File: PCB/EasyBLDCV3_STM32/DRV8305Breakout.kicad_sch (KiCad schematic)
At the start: 30 parts, among them Q1 CSD17573Q5B, Q2 CSD17573Q5B, Q3 CSD17573Q5B, Q4 CSD17573Q5B, Q5 CSD17573Q5B, Q6 CSD17573Q5B

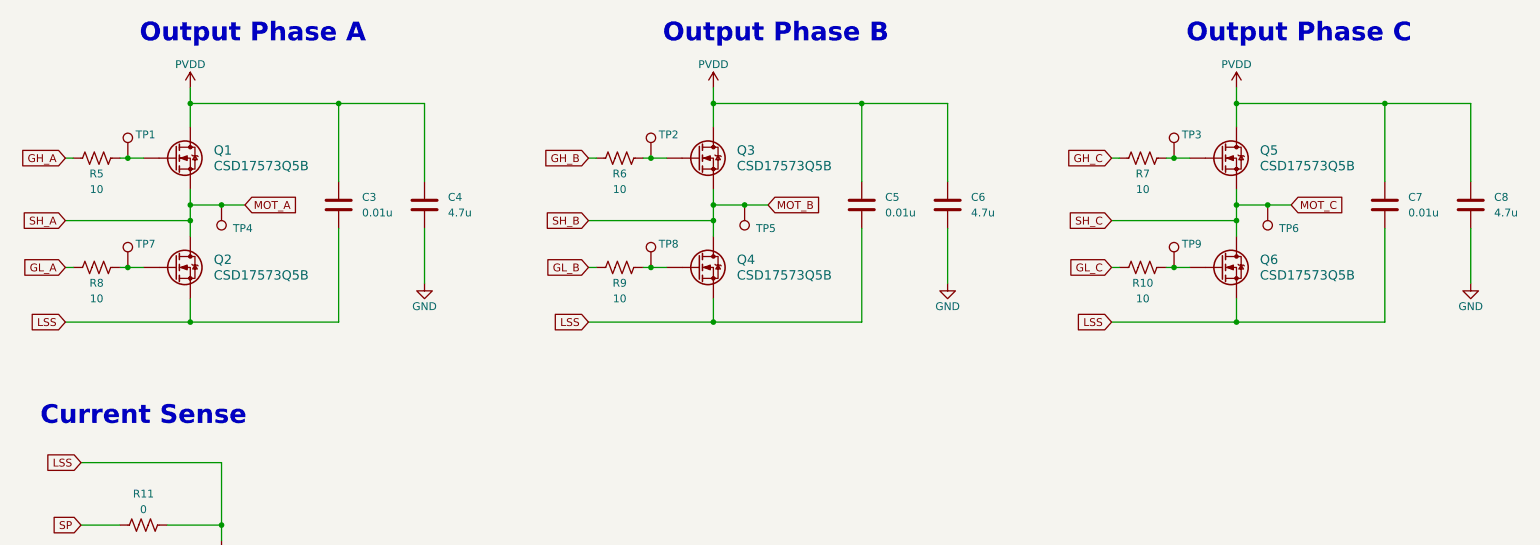
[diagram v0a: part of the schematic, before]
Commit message: Added footprints and began schematic for new gate drive
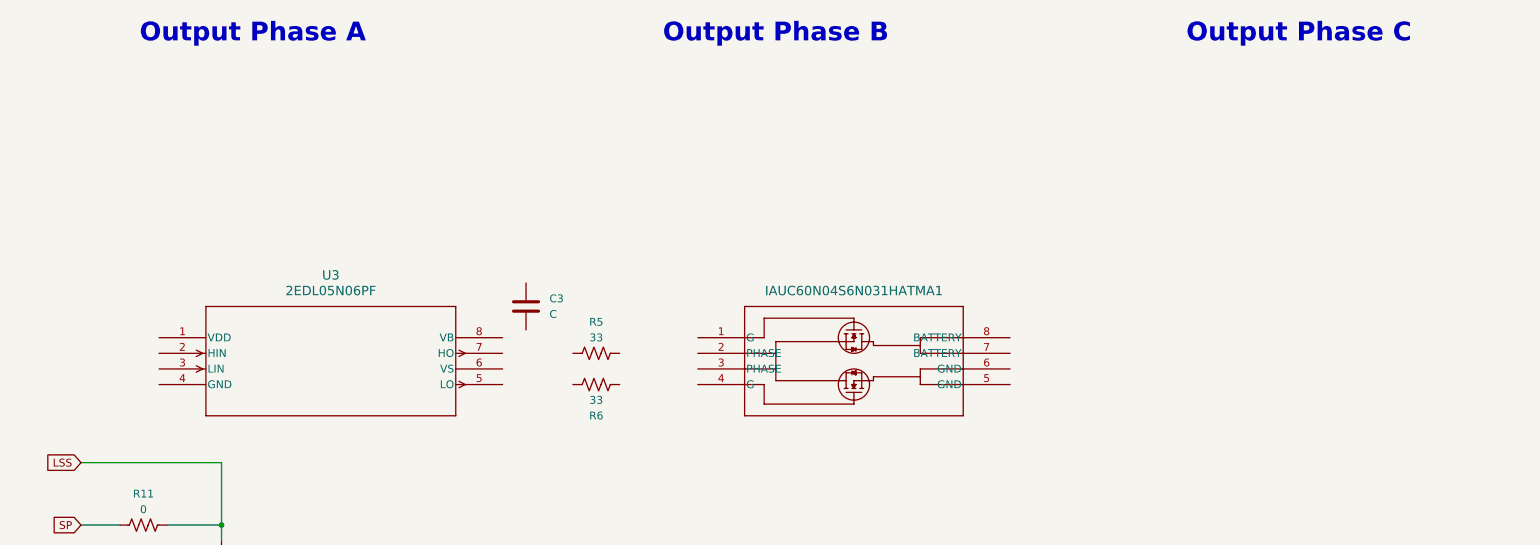
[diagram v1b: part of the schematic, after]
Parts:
- removed C4, C6, C8: 4.7u, Capacitor_SMD:C_1210_3225Metric, symbol Device:C
- removed C5, C7: 0.01u, Capacitor_SMD:C_0805_2012Metric, symbol Device:C
- removed Q1, Q2, Q3, Q4, Q5, Q6: CSD17573Q5B, EasyBLDC:DNK0008A, symbol EasyBLDC:CSD17573Q5B
- removed R10, R7, R8, R9: 10, Resistor_SMD:R_0603_1608Metric, symbol Device:R_US
- removed TP1, TP2, TP3, TP4, TP5, TP6, TP7, TP8, TP9: TestPoint, TestPoint:TestPoint_Pad_D1.5mm, symbol Connector:TestPoint
- added U2: IAUC60N04S6N031HATMA1, PG-TDSON-8-56, symbol EasyBLDC:IAUC60N04S6N031HATMA1
- added U3: 2EDL05N06PF, PG-DSO-8-1_INF, symbol EasyBLDC:2EDL05N06PF
- C3: value 0.01u -> C; footprint Capacitor_SMD:C_0805_2012Metric -> (none)
- R5, R6: value 10 -> 33
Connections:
- net LSS: no longer C3.2
- net GH_A: no longer names the net of R5.1
- net GH_B: no longer names the net of R6.1
- net PVDD: no longer names the net of C3.1
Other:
- note removed: "Current Sense"

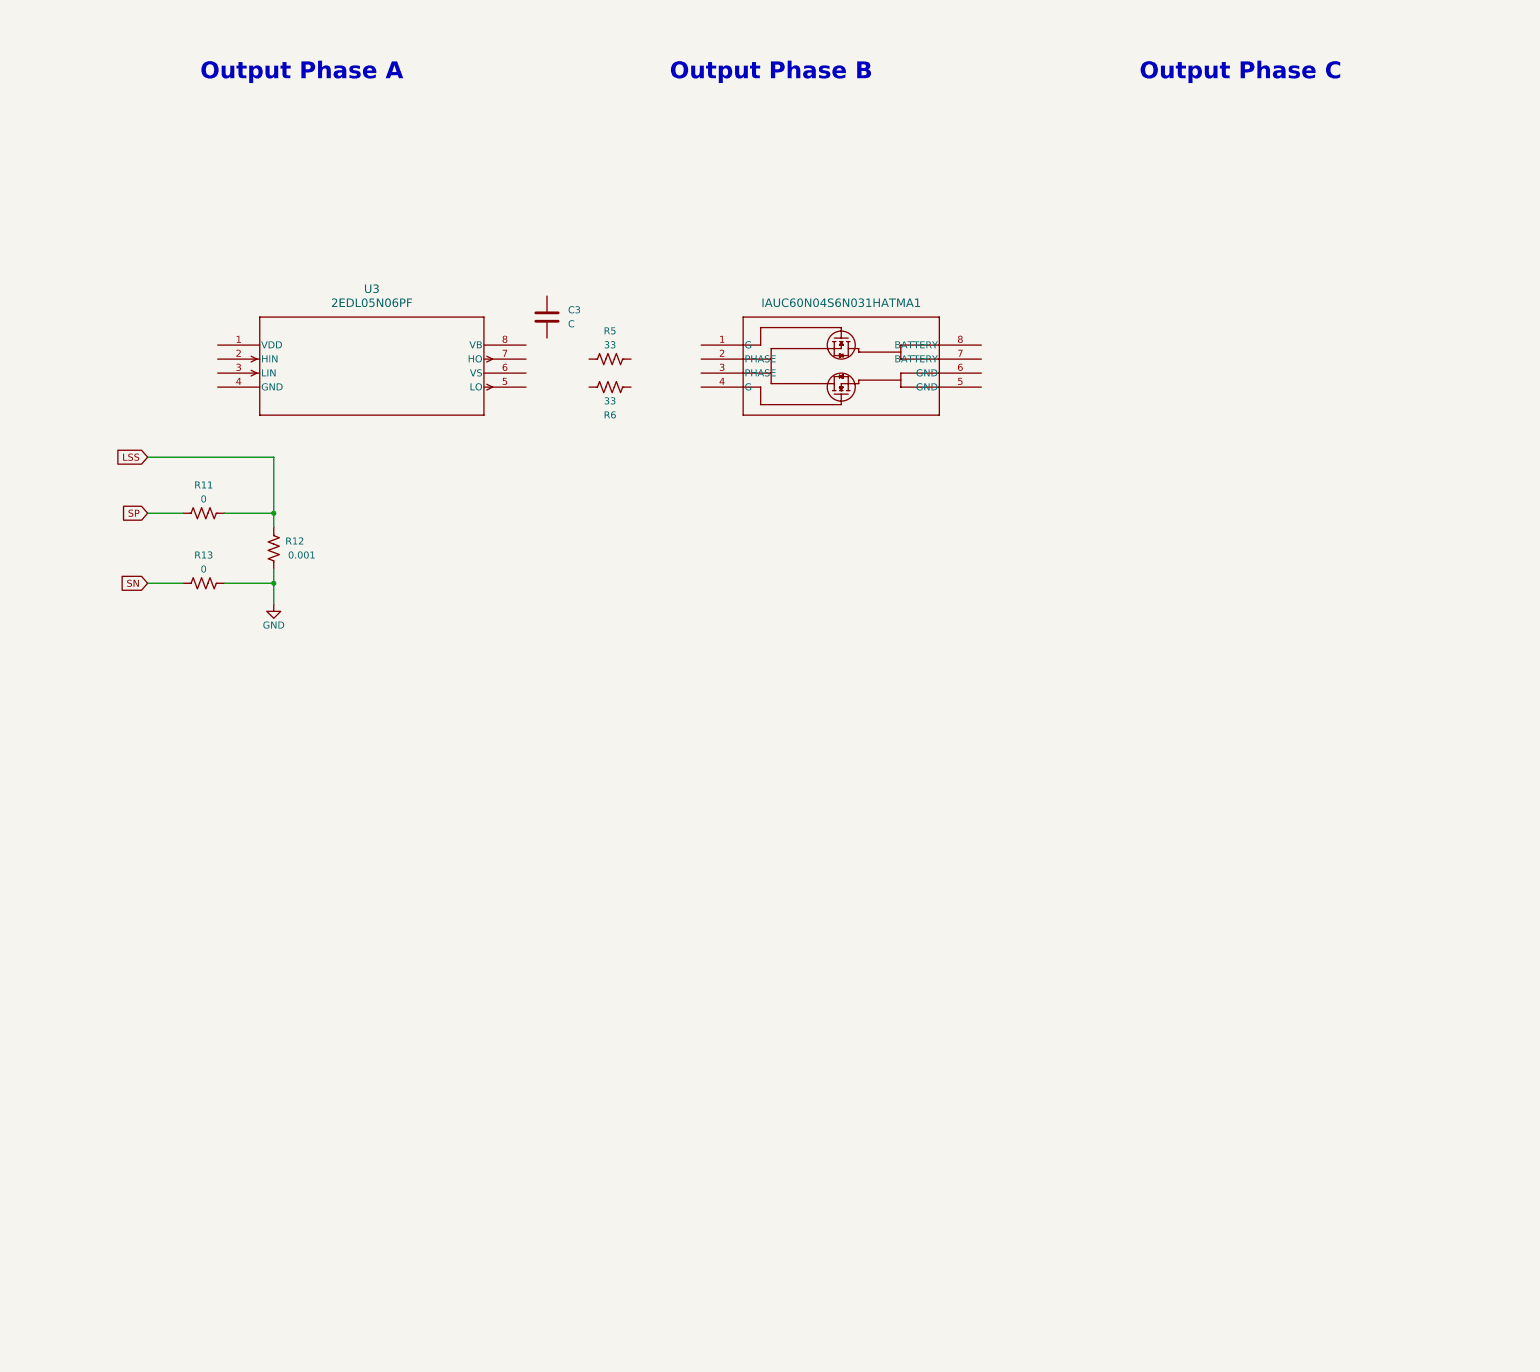
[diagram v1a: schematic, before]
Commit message: Worked on gate drive schematic
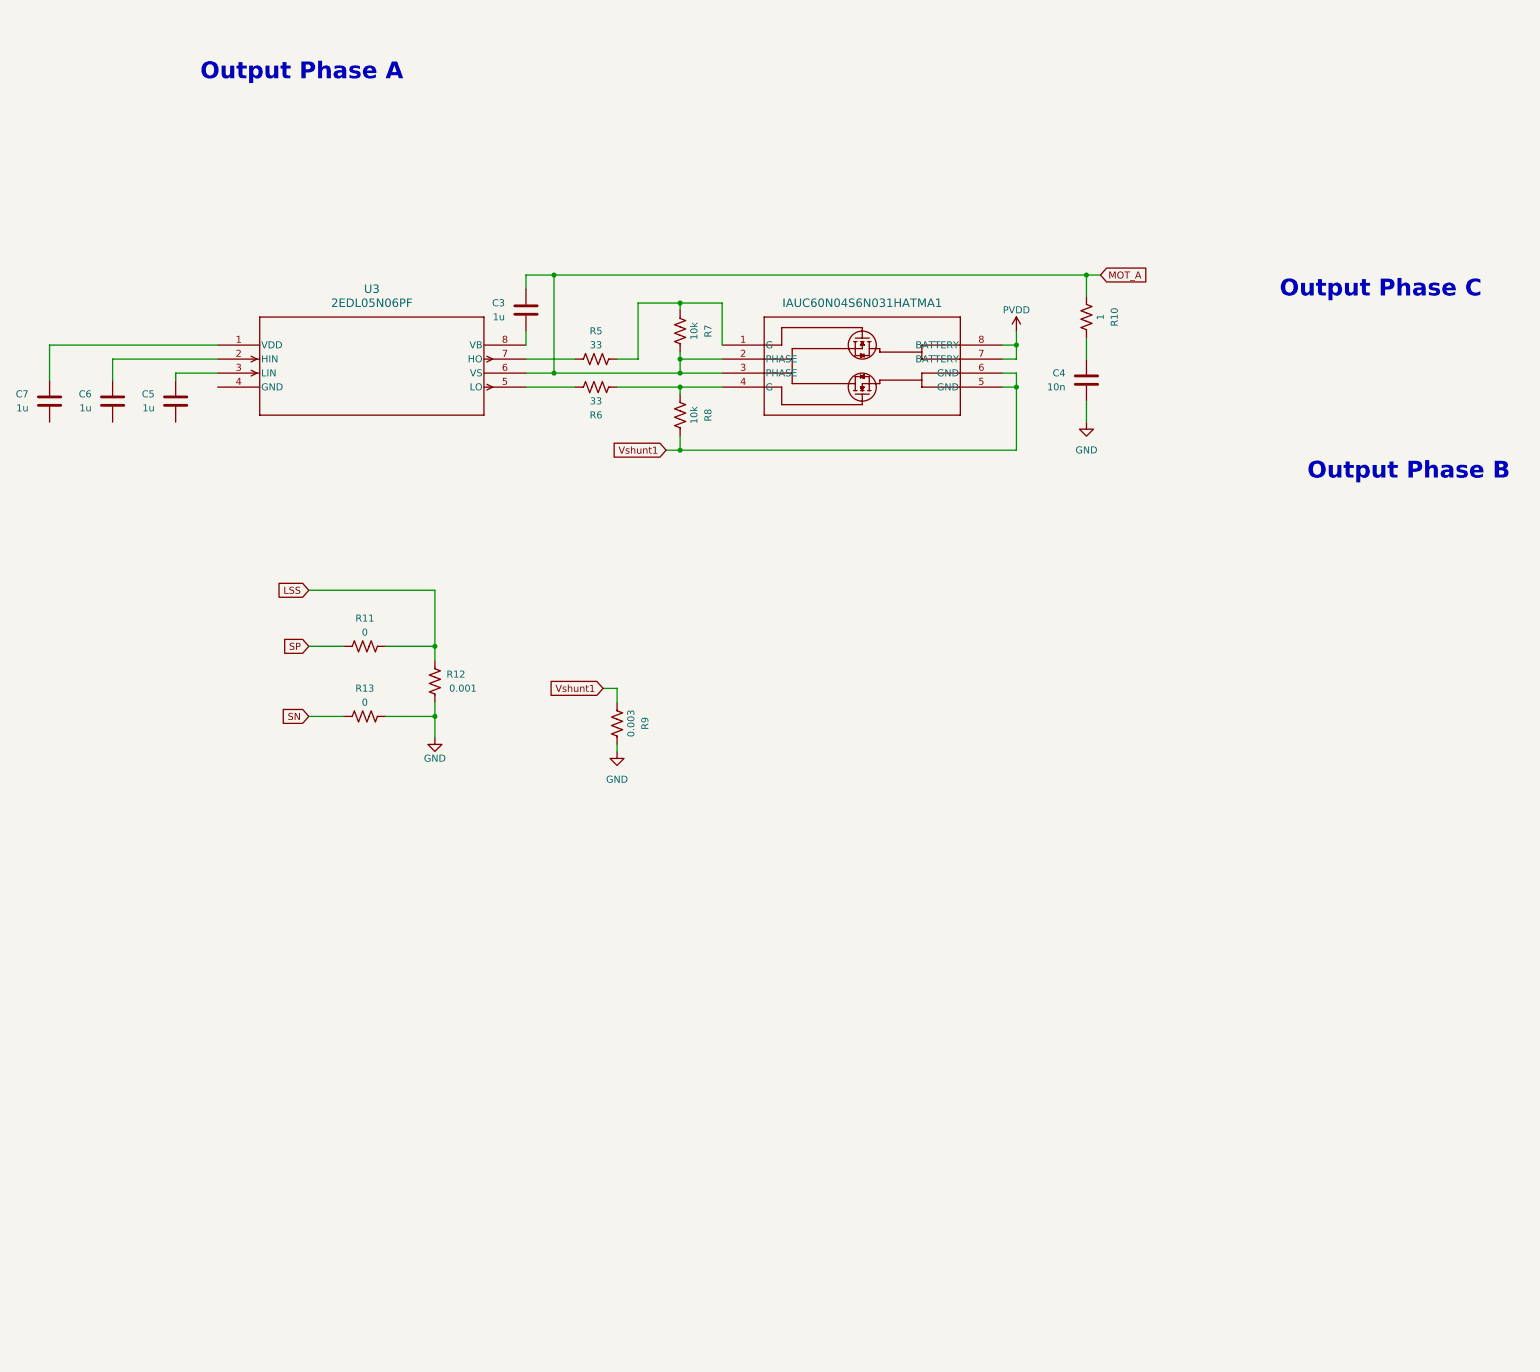
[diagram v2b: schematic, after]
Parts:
- added C4: 10n, symbol Device:C
- added C5, C6, C7: 1u, symbol Device:C
- added R10: 1, Resistor_SMD:R_0603_1608Metric, symbol Device:R_US
- added R7, R8: 10k, Resistor_SMD:R_0603_1608Metric, symbol Device:R_US
- added R9: 0.003, Resistor_SMD:R_0603_1608Metric, symbol Device:R_US
- C3: value C -> 1u
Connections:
- net GND: now also C4.1, R9.1
- net at R5.1: now also U2.1 (G), R7.2
- net at R5.2: now also U3.7 (HO)
- net MOT_A: now reaches U2.2 (PHASE)
- net MOT_A: now also C3.2, U2.3 (PHASE), U3.6 (VS), R10.2, R7.1
- net at U2.4 (G): now also R6.2, R8.2
- net Vshunt1: now reaches U2.5 (GND)
- net Vshunt1: now also U2.6 (GND), R8.1, R9.2
- net PVDD: now reaches U2.7 (BATTERY)
- net PVDD: now also U2.8 (BATTERY)
- net at C3.1: now also U3.8 (VB)
- net at U3.1 (VDD): now also C7.2
- net at U3.2 (HIN): now also C6.2
- net at U3.3 (LIN): now also C5.2
- net at U3.5 (LO): now also R6.1
- new net: C4.2, R10.1
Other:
- moved on the sheet: C3, R11, R12, R13, R5, R6

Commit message: Created V4 Project
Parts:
- added C10, C15: 770n, symbol Device:C
- added C11, C12, C16, C17: 100p, symbol Device:C
- added C13, C8: 1u, symbol Device:C
- added C14, C9: 10n, symbol Device:C
- added R14, R19: 1, Resistor_SMD:R_0603_1608Metric, symbol Device:R_US
- added R15, R18, R23, R26: 10k, Resistor_SMD:R_0603_1608Metric, symbol Device:R_US
- added R16, R17, R24, R25: 33, Resistor_SMD:R_0603_1608Metric, symbol Device:R_US
- added U4, U6: 2EDL05N06PF, PG-DSO-8-1_INF, symbol EasyBLDC:2EDL05N06PF
- added U5, U7: IAUC60N04S6N031HATMA1, PG-TDSON-8-56, symbol EasyBLDC:IAUC60N04S6N031HATMA1
- C5, C6: value 1u -> 100p
- C7: value 1u -> 770n
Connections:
- net GND: now also C5.1, C6.1, C7.1, U3.4 (GND), C10.1, C11.1, C12.1, C14.1, C15.1, C16.1, C17.1, C9.1, U4.4 (GND), U6.4 (GND)
- net PVDD: now also U5.7 (BATTERY), U5.8 (BATTERY), U7.7 (BATTERY), U7.8 (BATTERY)
- net Vshunt1: now also R18.1, R26.1, U5.5 (GND), U5.6 (GND), U7.5 (GND), U7.6 (GND)
- net TIM1_CHN1N: now reaches C5.2, U3.3 (LIN)
- net TIM1_CHN1N: now also C12.2, C17.2, U4.3 (LIN), U6.3 (LIN)
- net +10V: now reaches C7.2, U3.1 (VDD)
- net +10V: now also C10.2, C15.2, U4.1 (VDD), U6.1 (VDD)
- net TIM1_CHN1: now reaches C6.2, U3.2 (HIN)
- net TIM1_CHN1: now also C11.2, C16.2, U4.2 (HIN), U6.2 (HIN)
- net MOT_A renamed OUT1
- new net: C9.2, R14.1
- new net: C13.1, U6.8 (VB)
- new net: C14.2, R19.1
- new net: R17.1, U4.5 (LO)
- new net: R17.2, R18.2, U5.4 (G)
- new net: R23.2, R24.1, U7.1 (G)
- new net: R15.2, R16.1, U5.1 (G)
- new net: R16.2, U4.7 (HO)
- new net: R25.2, R26.2, U7.4 (G)
- new net: C8.1, U4.8 (VB)
- new net: R25.1, U6.5 (LO)
- new net: R24.2, U6.7 (HO)
- new net OUT2: C8.2, R14.2, R15.1, U4.6 (VS), U5.2 (PHASE), U5.3 (PHASE)
- new net OUT3: C13.2, R19.2, R23.1, U6.6 (VS), U7.2 (PHASE), U7.3 (PHASE)
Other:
- moved on the sheet: C3, C4, C5, C6, C7, R10, R11, R12, R13, R5, R6, R7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
